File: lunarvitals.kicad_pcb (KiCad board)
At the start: 2 copper layers, 48.5 x 35 mm, 44 parts, among them J1 ConductiveCord, J2 MPU6050, J3 SEN11574, J4 MAX30102, J5 USB_C_Receptacle_PowerOnly_6P, J6 Battery, J7 Conn_01x07, Q1 FS8205, SW1 SW_SPDT, U1 NRF52840-DONGLE, U3 AP2112K-3.3, U4 TP4056, U5 MLX90614ESF-AAA-000-TU, U6 DW01A

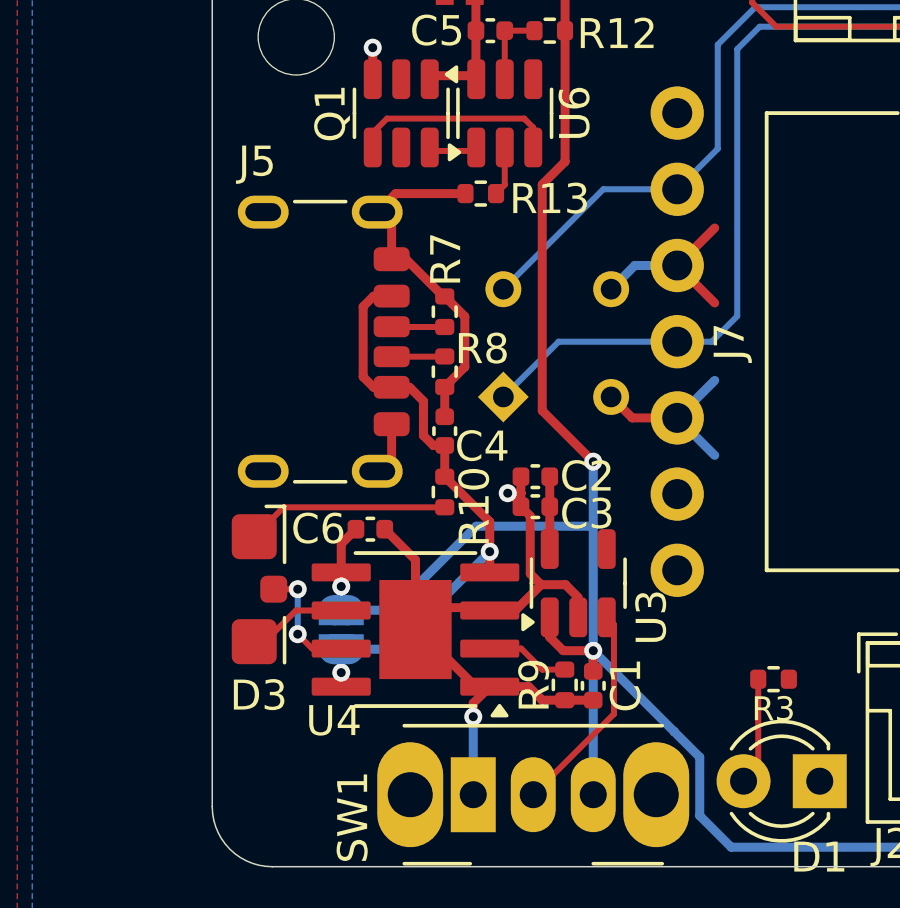
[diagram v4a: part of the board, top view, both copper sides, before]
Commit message: dual led location and routing fix
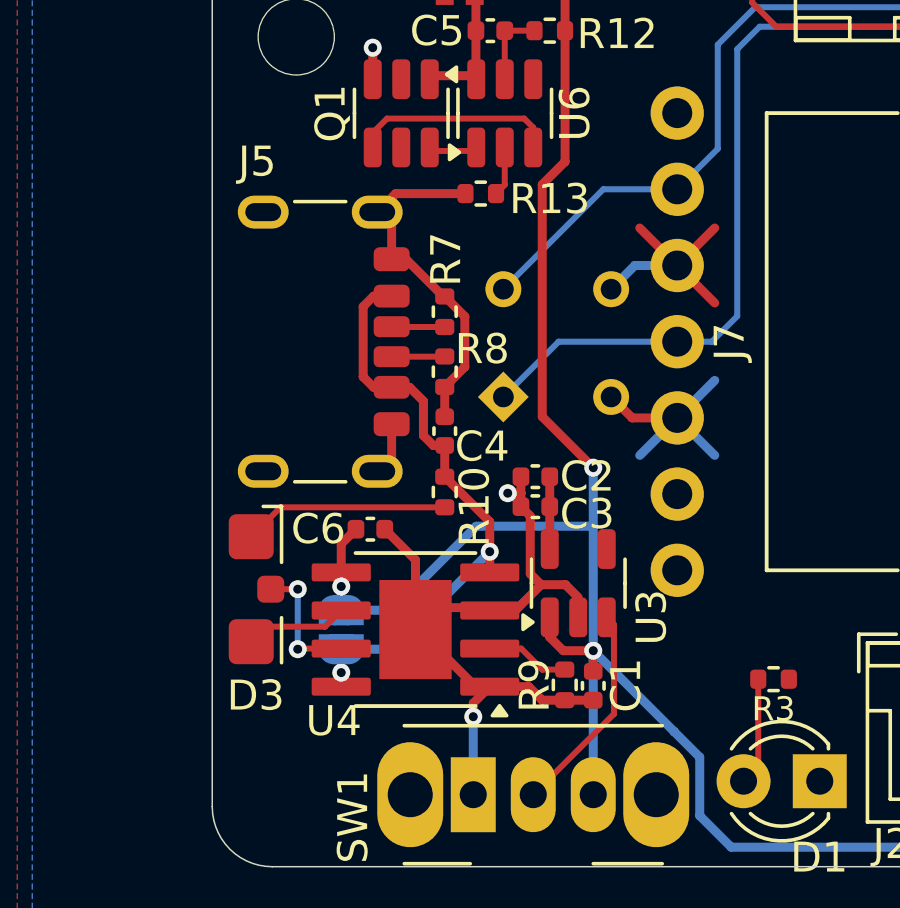
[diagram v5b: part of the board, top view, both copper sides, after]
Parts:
- moved D3 0.10 mm to (141.8, 118.2)
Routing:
- net GND: track 54.3 -> 56.0 mm
- net +3.3V: track 10.9 -> 12.6 mm
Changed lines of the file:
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@@
 	(footprint "lunar_vitals_custom:LED_Kingbright_APBA3010SURKCGKC-GX_3x2x1mm"
 		(layer "F.Cu")
-		(at 141.9 118.25 90)
+		(at 141.8 118.25 90)
 		(descr "Kingbright surface mount LED, right angle, 3.0 x 2.0 x 1.0 mm, https://www.kingbright.com/attachments/file/psearch/000/00/00/KPA-3010SURCK(Ver.26A).pdf")
 		(tags "Kingbright LED right-angle")
@@
 			(thermal_bridge_angle 0)
 		)
-		(model "C:/Users/Zeiler/Documents/UCSBCapstone/PCB/bmp280breakout/bmp280_breakout.step"
+		(model "${KIPRJMOD}/customlib/bmp280_breakout.step"
 			(offset
 				(xyz -12.7 -8.89 3.5)
@@
 	)
 	(segment
+		(start 152 112.5)
+		(end 152 104.76)
+		(width 0.3)
+		(layer "F.Cu")
+		(net 2)
+	)
+	(segment
 		(start 145.3 116.74)
 		(end 145.79 116.25)
@@
 	)
 	(segment
-		(start 152.76 104)
-		(end 152.76 99.6325)
-		(width 0.3)
-		(layer "F.Cu")
-		(net 2)
-	)
-	(segment
-		(start 152 112.3)
-		(end 152 104.76)
-		(width 0.3)
-		(layer "F.Cu")
-		(net 2)
-	)
-	(segment
 		(start 152.76 97.235)
 		(end 152.76 99.6325)
@@
 	)
 	(segment
-		(start 152 104.76)
-		(end 152.76 104)
+		(start 153.7 114.2)
+		(end 152 112.5)
 		(width 0.3)
 		(layer "F.Cu")
@@
 	)
 	(segment
-		(start 152.75 99.6225)
+		(start 152.76 104)
 		(end 152.76 99.6325)
 		(width 0.3)
@@
 	)
 	(segment
-		(start 153.7 114)
-		(end 152 112.3)
+		(start 152.75 99.6225)
+		(end 152.76 99.6325)
 		(width 0.3)
 		(layer "F.Cu")
@@
 	)
 	(segment
+		(start 152 104.76)
+		(end 152.76 104)
+		(width 0.3)
+		(layer "F.Cu")
+		(net 2)
+	)
+	(segment
 		(start 149.1 96.875)
 		(end 152.4 96.875)
@@
 	)
 	(via
-		(at 153.7 114)
+		(at 153.7 114.2)
 		(size 0.6)
 		(drill 0.3)
@@
 	)
 	(segment
-		(start 157.25 123.84939)
-		(end 157.25 125.8)
+		(start 153.7 114.2)
+		(end 153.7 116.15)
 		(width 0.3)
 		(layer "B.Cu")
@@
 	)
 	(segment
-		(start 153.7 114)
-		(end 153.7 116.15)
+		(start 157.25 123.84939)
+		(end 157.25 125.8)
 		(width 0.3)
 		(layer "B.Cu")
@@
 	)
 	(segment
+		(start 156.5 107.46)
+		(end 155.25 106.21)
+		(width 0.3)
+		(layer "F.Cu")
+		(net 4)
+	)
+	(segment
 		(start 152.25 114.5)
 		(end 152.25 115.5)
@@
 	)
 	(segment
-		(start 142.5 120)
-		(end 142.75 120)
+		(start 144.76 119.5)
+		(end 145.3 118.96)
 		(width 0.2)
 		(layer "F.Cu")
@@
 	)
 	(segment
-		(start 143.79 118.96)
-		(end 145.3 118.96)
+		(start 142.3 120)
+		(end 142.8 119.5)
 		(width 0.2)
 		(layer "F.Cu")
@@
 	)
 	(segment
-		(start 142.75 120)
-		(end 143.79 118.96)
+		(start 142.8 119.5)
+		(end 144.76 119.5)
 		(width 0.2)
 		(layer "F.Cu")
@@
 	)
 	(segment
-		(start 143.85 118.25)
-		(end 143.05 118.25)
+		(start 143.87 120.23)
+		(end 145.3 120.23)
 		(width 0.2)
 		(layer "F.Cu")
@@
 	)
 	(segment
-		(start 144.33 120.23)
-		(end 145.3 120.23)
+		(start 143.85 118.25)
+		(end 142.95 118.25)
 		(width 0.2)
 		(layer "F.Cu")
@@
 	)
 	(segment
-		(start 143.849265 119.749265)
-		(end 144.33 120.23)
+		(start 143.85 120.25)
+		(end 143.87 120.23)
 		(width 0.2)
 		(layer "F.Cu")
@@
 	)
 	(via
-		(at 143.849265 119.749265)
+		(at 143.85 120.25)
 		(size 0.6)
 		(drill 0.3)
@@
 	)
 	(segment
-		(start 143.849265 119.749265)
-		(end 143.849265 118.250735)
-		(width 0.2)
-		(layer "B.Cu")
-		(net 9)
-	)
-	(segment
-		(start 143.849265 118.250735)
-		(end 143.85 118.25)
-		(width 0.2)
-		(layer "B.Cu")
-		(net 9)
-	)
-	(segment
-		(start 143.874265 118.274265)
-		(end 143.85 118.25)
+		(start 143.85 118.25)
+		(end 143.85 120.25)
 		(width 0.2)
 		(layer "B.Cu")
@@
 	(segment
 		(start 148.75 115.52)
-		(end 143.38 115.52)
+		(end 143.28 115.52)
 		(width 0.2)
 		(layer "F.Cu")
@@
 	)
 	(segment
-		(start 143.38 115.52)
-		(end 142.4 116.5)
+		(start 143.28 115.52)
+		(end 142.3 116.5)
 		(width 0.2)
 		(layer "F.Cu")
@@
 		(width 0.3)
 		(layer "B.Cu")
+		(net 34)
+	)
+	(segment
+		(start 156.5 112.54)
+		(end 155.25 113.79)
+		(width 0.3)
+		(layer "B.Cu")

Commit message: move LED footprint anchor
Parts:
- moved D3 0.50 mm to (142.3, 118.2)
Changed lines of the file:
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@@
 	(footprint "lunar_vitals_custom:LED_Kingbright_APBA3010SURKCGKC-GX_3x2x1mm"
 		(layer "F.Cu")
-		(at 141.8 118.25 90)
+		(at 142.3 118.25 90)
 		(descr "Kingbright surface mount LED, right angle, 3.0 x 2.0 x 1.0 mm, https://www.kingbright.com/attachments/file/psearch/000/00/00/KPA-3010SURCK(Ver.26A).pdf")
 		(tags "Kingbright LED right-angle")
 		(property "Reference" "D3"
-			(at -3.55 0.65 180)
+			(at -3.55 0.15 180)
 			(layer "F.SilkS")
 			(effects
@@
 		(attr smd)
 		(fp_line
-			(start 2.76 0.9)
-			(end 2.76 1.51)
+			(start 2.76 0.4)
+			(end 2.76 1.01)
 			(stroke
 				(width 0.12)
@@
 		)
 		(fp_line
-			(start 0.895 1.51)
-			(end 2.76 1.51)
+			(start 0.895 1.01)
+			(end 2.76 1.01)
 			(stroke
 				(width 0.12)
@@
 		)
 		(fp_line
-			(start -2.45 1.51)
-			(end -0.95 1.51)
+			(start -2.45 1.01)
+			(end -0.95 1.01)
 			(stroke
 				(width 0.12)
@@
 		)
 		(fp_line
-			(start 1.5 -1.25)
+			(start 1.5 -1.75)
+			(end 1.5 -1)
+			(stroke
+				(width 0.05)
+				(type default)
+			)
+			(layer "F.CrtYd")
+		)
+		(fp_line
+			(start -1.5 -1.75)
+			(end 1.5 -1.75)
+			(stroke
+				(width 0.05)
+				(type default)
+			)
+			(layer "F.CrtYd")
+		)
+		(fp_line
+			(start -1.5 -1.75)
+			(end -1.5 -1)
+			(stroke
+				(width 0.05)
+				(type default)
+			)
+			(layer "F.CrtYd")
+		)
+		(fp_line
+			(start 2.75 -1)
+			(end 2.75 1)
+			(stroke
+				(width 0.05)
+				(type default)
+			)
+			(layer "F.CrtYd")
+		)
+		(fp_line
+			(start 1.5 -1)
+			(end 2.75 -1)
+			(stroke
+				(width 0.05)
+				(type default)
+			)
+			(layer "F.CrtYd")
+		)
+		(fp_line
+			(start -1.5 -1)
+			(end -2.75 -1)
+			(stroke
+				(width 0.05)
+				(type default)
+			)
+			(layer "F.CrtYd")
+		)
+		(fp_line
+			(start 2.75 1)
+			(end 0.7 1)
+			(stroke
+				(width 0.05)
+				(type default)
+			)
+			(layer "F.CrtYd")
+		)
+		(fp_line
+			(start 0.7 1)
+			(end 0.7 1.35)
+			(stroke
+				(width 0.05)
+				(type default)
+			)
+			(layer "F.CrtYd")
+		)
+		(fp_line
+			(start -0.7 1)
+			(end -2.75 1)
+			(stroke
+				(width 0.05)
+				(type default)
+			)
+			(layer "F.CrtYd")
+		)
+		(fp_line
+			(start -2.75 1)
+			(end -2.75 -1)
+			(stroke
+				(width 0.05)
+				(type default)
+			)
+			(layer "F.CrtYd")
+		)
+		(fp_line
+			(start 0.7 1.35)
+			(end -0.7 1.35)
+			(stroke
+				(width 0.05)
+				(type default)
+			)
+			(layer "F.CrtYd")
+		)
+		(fp_line
+			(start -0.7 1.35)
+			(end -0.7 1)
+			(stroke
+				(width 0.05)
+				(type default)
+			)
+			(layer "F.CrtYd")
+		)
+		(fp_line
+			(start -0.5 -1.5)
+			(end 0.5 -1.5)
+			(stroke
+				(width 0.1)
+				(type solid)
+			)
+			(layer "F.Fab")
+		)
+		(fp_line
+			(start 1 -1)
+			(end 1 -0.5)
+			(stroke
+				(width 0.1)
+				(type solid)
+			)
+			(layer "F.Fab")
+		)
+		(fp_line
+			(start 1.5 -0.5)
+			(end 1.5 0.5)
+			(stroke
+				(width 0.1)
+				(type solid)
+			)
+			(layer "F.Fab")
+		)
+		(fp_line
+			(start -1 -0.5)
+			(end -1 -1)
+			(stroke
+				(width 0.1)
+				(type solid)
+			)
+			(layer "F.Fab")
+		)
+		(fp_line
+			(start -1.2 -0.5)
+			(end -1.2 0.5)
+			(stroke
+				(width 0.1)
+				(type solid)
+			)
+			(layer "F.Fab")
+		)
+		(fp_line
+			(start -1.5 -0.5)
 			(end 1.5 -0.5)
 			(stroke
-				(width 0.05)
-				(type default)
-			)
-			(layer "F.CrtYd")
-		)
-		(fp_line
-			(start -1.5 -1.25)
-			(end 1.5 -1.25)
-			(stroke
-				(width 0.05)
-				(type default)
-			)
-			(layer "F.CrtYd")
-		)
-		(fp_line
-			(start -1.5 -1.25)
+				(width 0.1)
+				(type solid)
+			)
+			(layer "F.Fab")
+		)
+		(fp_line
+			(start 1.5 0.5)
+			(end -1.5 0.5)
+			(stroke
+				(width 0.1)
+				(type solid)
+			)
+			(layer "F.Fab")
+		)
+		(fp_line
+			(start -1.5 0.5)
 			(end -1.5 -0.5)
 			(stroke
-				(width 0.05)
-				(type default)
-			)
-			(layer "F.CrtYd")
-		)
-		(fp_line
-			(start 2.75 -0.5)
-			(end 2.75 1.5)
-			(stroke
-				(width 0.05)
-				(type default)
-			)
-			(layer "F.CrtYd")
-		)
-		(fp_line
-			(start 1.5 -0.5)
-			(end 2.75 -0.5)
-			(stroke
-				(width 0.05)
-				(type default)
-			)
-			(layer "F.CrtYd")
-		)
-		(fp_line
-			(start -1.5 -0.5)
-			(end -2.75 -0.5)
-			(stroke
-				(width 0.05)
-				(type default)
-			)
-			(layer "F.CrtYd")
-		)
-		(fp_line
-			(start 2.75 1.5)
-			(end 0.7 1.5)
-			(stroke
-				(width 0.05)
-				(type default)
-			)
-			(layer "F.CrtYd")
-		)
-		(fp_line
-			(start 0.7 1.5)
-			(end 0.7 1.85)
-			(stroke
-				(width 0.05)
-				(type default)
-			)
-			(layer "F.CrtYd")
-		)
-		(fp_line
-			(start -0.7 1.5)
-			(end -2.75 1.5)
-			(stroke
-				(width 0.05)
-				(type default)
-			)
-			(layer "F.CrtYd")
-		)
-		(fp_line
-			(start -2.75 1.5)
-			(end -2.75 -0.5)
-			(stroke
-				(width 0.05)
-				(type default)
-			)
-			(layer "F.CrtYd")
-		)
-		(fp_line
-			(start 0.7 1.85)
-			(end -0.7 1.85)
-			(stroke
-				(width 0.05)
-				(type default)
-			)
-			(layer "F.CrtYd")
-		)
-		(fp_line
-			(start -0.7 1.85)
-			(end -0.7 1.5)
-			(stroke
-				(width 0.05)
-				(type default)
-			)
-			(layer "F.CrtYd")
-		)
-		(fp_line
-			(start -0.5 -1)
-			(end 0.5 -1)
-			(stroke
-				(width 0.1)
-				(type solid)
-			)
-			(layer "F.Fab")
-		)
-		(fp_line
-			(start 1 -0.5)
-			(end 1 0)
-			(stroke
-				(width 0.1)
-				(type solid)
-			)
-			(layer "F.Fab")
-		)
-		(fp_line
-			(start 1.5 0)
-			(end 1.5 1)
-			(stroke
-				(width 0.1)
-				(type solid)
-			)
-			(layer "F.Fab")
-		)
-		(fp_line
-			(start -1 0)
-			(end -1 -0.5)
-			(stroke
-				(width 0.1)
-				(type solid)
-			)
-			(layer "F.Fab")
-		)
-		(fp_line
-			(start -1.2 0)
-			(end -1.2 1)
-			(stroke
-				(width 0.1)
-				(type solid)
-			)
-			(layer "F.Fab")
-		)
-		(fp_line
-			(start -1.5 0)
-			(end 1.5 0)
-			(stroke
-				(width 0.1)
-				(type solid)
-			)
-			(layer "F.Fab")
-		)
-		(fp_line
-			(start 1.5 1)
-			(end -1.5 1)
-			(stroke
-				(width 0.1)
-				(type solid)
-			)
-			(layer "F.Fab")
-		)
-		(fp_line
-			(start -1.5 1)
-			(end -1.5 0)
-			(stroke
 				(width 0.1)
 				(type solid)
@@
 		)
 		(fp_arc
-			(start 0.5 -1)
-			(mid 0.853553 -0.853553)
-			(end 1 -0.5)
+			(start 0.5 -1.5)
+			(mid 0.853553 -1.353553)
+			(end 1 -1)
 			(stroke
 				(width 0.1)
@@
 		)
 		(fp_arc
-			(start -1 -0.5)
-			(mid -0.853553 -0.853553)
-			(end -0.5 -1)
+			(start -1 -1)
+			(mid -0.853553 -1.353553)
+			(end -0.5 -1.5)
 			(stroke
 				(width 0.1)
@@
 		)
 		(pad "1" smd roundrect
-			(at 1.75 0.5 90)
+			(at 1.75 0 90)
 			(size 1.5 1.5)
 			(layers "F.Cu" "F.Paste" "F.Mask")
@@
 		)
 		(pad "2" smd roundrect
-			(at 0 1.15 90)
+			(at 0 0.65 90)
 			(size 0.9 0.9)
 			(layers "F.Cu" "F.Paste" "F.Mask")
@@
 		)
 		(pad "3" smd roundrect
-			(at -1.75 0.5 90)
+			(at -1.75 0 90)
 			(size 1.5 1.5)
 			(layers "F.Cu" "F.Paste" "F.Mask")
@@
 		(model "${KIPRJMOD}/customlib/APBA3010-APBA3010.step"
 			(offset
-				(xyz 0 -0.5 0)
+				(xyz 0 0 0)
 			)
 			(scale
